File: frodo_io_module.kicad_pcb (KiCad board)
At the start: 4 copper layers, 60 x 60 mm, 174 parts, among them J1 Conn_02x04_Top_Bottom, J10 JST-GH 4Pin, J11 JST-GH 4Pin, J14 Conn_02x03_Odd_Even, J16 USB_C_Receptacle_USB2.0, J17 TC2050, J2 Conn_02x10_Odd_Even, J3 Conn_02x04_Top_Bottom, J4 Conn_02x03_Odd_Even, J5 Conn_02x04_Odd_Even, J6 JST-GH 4Pin, J7 JST-GH 4Pin, J8 JST-GH 4Pin, J9 JST-GH 4Pin, Q1 AOSP21321, Q2 AOSP21321, Q3 NMOS, Q4 NMOS, Q5 AOSP21321, Q6 AOSP21321, Q7 NMOS, Q8 NMOS, SW1 KMR721NGLFS, SW2 KMR721NGLFS, SW3 KMR721NGLFS, U1 L7805, U10 MCP2562-E-SN, U11 TPD4E1U06, U12 INA181A1, U2 L7805, U3 STM32F105RCTx, U4 AZ1117H-ADJ, U5 AZ1117H-ADJ, U6 W25Q128JVP, U7 MCP2562-E-SN, U8 TPD4E1U06, U9 INA181A1, Y1 8MHz 12pF

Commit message: rough placement of the components
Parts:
- C29, D10, D12, D13, D14, D16, D18, D19, D9, F2, F3, FB10, FB12, FB13, FB2, FB3, FB5, FB6, FB9, J17, Q1, Q2, Q3, Q4, Q5, Q6, Q7, Q8, R15, R17, R26, R30, R32, R33, R4, R41, R46, R47, R5, R52, R53, R54, R55, R56, R57, R58, R59, R60, R61, R62, R63, SW1, SW2, SW3, U11: moved to B.Cu
- moved D11 188.4 mm to (103.8, 137.7), turned to 90 degrees
- moved D7 186.7 mm to (103.8, 148.0), turned to 90 degrees
- moved U6 184.7 mm to (127.0, 141.4)
- moved D6 182.5 mm to (107.4, 140.5)
- moved D5 180.9 mm to (103.8, 127.8), turned to 90 degrees
- moved D9 168.1 mm to (114.1, 106.3), turned to 90 degrees
- moved D8 165.6 mm to (115.5, 134.1), turned to 90 degrees
- moved D14 164.2 mm to (141.0, 142.3), turned to -90 degrees
- moved D10 164.1 mm to (115.9, 106.4), turned to 90 degrees
- moved D13 163.6 mm to (141.7, 136.8)
- moved D3 161.3 mm to (103.7, 119.1), turned to 90 degrees
- moved D12 157.3 mm to (117.6, 106.4), turned to 90 degrees
- moved C1 154.2 mm to (124.0, 131.9), turned to 90 degrees
- moved D2 151.3 mm to (117.4, 115.7), turned to 90 degrees
- moved C22 150.7 mm to (128.7, 145.6)
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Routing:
- net Net-(D8-A): track 0.00 -> 21.1 mm
- net NRST: track 11.7 -> 0.00 mm
- net /VBUS: track 12.8 -> 6.15 mm
- net USB_D-: track 0.00 -> 5.91 mm
- net USB_D+: track 0.00 -> 5.91 mm
- net GND: track 10.2 -> 5.59 mm
- net Net-(U5-GND): track 0.00 -> 3.89 mm
- net unconnected-(J16-SBU2-PadB8): track 3.79 -> 0.00 mm
- net /D0+: track 3.83 -> 7.32 mm, vias 1 -> 2
- net +3.3V: track 16.8 -> 14.6 mm
- net Net-(J16-CC1): track 0.00 -> 1.92 mm, vias 0 -> 1
- net Net-(D11-A): track 0.00 -> 1.58 mm
- net Net-(J16-CC2): track 0.76 -> 2.22 mm
- net /D0-: track 8.54 -> 7.46 mm
- net (no net): track 0.99 -> 0.00 mm
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
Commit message: basic routing
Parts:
- C1, C10, C2, C20, C21, C22, C26, C3, C4, C5, C6, C7, C8, C9, D11, D3, D5, D7, FB1, FB11, FB4, FB7, FB8, R10, R11, R12, R13, R14, R18, R19, R20, R21, R22, R23, R25, R27, R31, R35, R36, R38, R39, R42, R48, R8, R9, U12, U3, U6, U8, U9, Y1: moved to B.Cu
- D13, D14, D16, D18, D19, F2, F3, J2, Q1, Q2, Q3, Q4, Q5, Q6, Q7, Q8, R15, R17, R4, R5, R52, R53, R55, R57, R58, R59, R60, R61, R62, R63: moved to F.Cu
- moved D7 42.9 mm to (119.0, 107.8), turned to -90 degrees
- moved C18 35.7 mm to (102.6, 148.0)
- moved D11 32.8 mm to (117.5, 107.8), turned to -90 degrees
- moved C22 32.2 mm to (127.0, 113.4), turned to 90 degrees
- moved R18 32.1 mm to (107.5, 128.1), turned to 90 degrees
- moved R19 31.7 mm to (107.4, 148.2), turned to 90 degrees
- moved R21 31.5 mm to (107.5, 122.0), turned to -90 degrees
- moved R13 29.9 mm to (107.5, 131.8), turned to -90 degrees
- moved C15 28.4 mm to (138.5, 105.1)
- moved C28 27.3 mm to (110.8, 111.8), turned to 0 degrees
- moved U6 26.3 mm to (123.4, 115.3), turned to 90 degrees
- moved R22 25.3 mm to (107.4, 141.9), turned to -90 degrees
- moved R31 24.7 mm to (119.1, 134.2), turned to 180 degrees
- moved C30 24.6 mm to (118.0, 136.2), turned to 180 degrees
- moved D5 23.4 mm to (116.0, 107.8), turned to -90 degrees
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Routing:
- net CAN_2_L: track 0.00 -> 110.1 mm, vias 0 -> 1
- net /Digital Output/OUT2: track 0.00 -> 107.2 mm, vias 0 -> 2
- net /Digital Output1/OUT1: track 0.00 -> 91.2 mm, vias 0 -> 2
- net CAN_2_H: track 0.00 -> 88.3 mm, vias 0 -> 3
- net /Digital Output1/OUT2: track 0.00 -> 88.0 mm, vias 0 -> 1
- net /Digital Output/OUT1: track 0.00 -> 84.0 mm, vias 0 -> 2
- net SWCLK: track 0.00 -> 73.3 mm, vias 0 -> 2
- net CAN_1_L: track 0.00 -> 64.2 mm, vias 0 -> 1
- net BOOT: track 0.00 -> 62.3 mm, vias 0 -> 3
- net CAN_1_H: track 0.00 -> 62.3 mm, vias 0 -> 1
- net NRST: track 0.00 -> 60.4 mm, vias 0 -> 5
- net COM4_1: track 0.00 -> 54.2 mm, vias 0 -> 2
- net Net-(D7-A): track 0.00 -> 53.6 mm, vias 0 -> 2
- net SWDIO: track 0.00 -> 48.9 mm
- net COM1_2: track 0.00 -> 48.7 mm, vias 0 -> 2
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
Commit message: more routing
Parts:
- moved R62 4.32 mm to (118.3, 124.5), turned to 180 degrees
- moved C25 2.86 mm to (123.3, 113.8)
- moved C11 2.40 mm to (112.5, 121.4)
- moved Q3 1.49 mm to (129.3, 123.4)
- moved J2 1.28 mm to (130.9, 115.9)
- moved D18 1.13 mm to (118.8, 143.2)
- moved D2 0.61 mm to (115.3, 119.0)
- moved R37 0.50 mm to (132.4, 104.1)
- moved D19 0.48 mm to (115.1, 157.0)
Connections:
- D13 pad 1: v_main_pre_sense -> main_voltage
- D14 pad 1: v_main_pre_sense -> main_voltage
- U3 pad 24: AIN2 -> AIN3
- U3 pad 25: AIN3 -> AIN2
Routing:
- net /Digital Output1/OUT1: track 91.2 -> 68.5 mm, vias 2 -> 3
- net CAN_2_L: track 110.1 -> 87.9 mm, vias 1 -> 3
- net CAN_2_H: track 88.3 -> 67.6 mm, vias 3 -> 0
- net NRST: track 60.4 -> 78.6 mm, vias 5 -> 10
- net COM2_1: track 31.6 -> 48.8 mm
- net COM4_2: track 48.1 -> 63.4 mm, vias 2 -> 0
- net SPI_CS_FLASH: track 0.00 -> 14.9 mm, vias 0 -> 2
- net STAT_LED0: track 48.4 -> 34.2 mm
- net /Digital Output1/OUT2: track 88.0 -> 101.4 mm, vias 1 -> 3
- net STAT_LED1: track 48.0 -> 35.8 mm
- net COM4_1: track 54.2 -> 64.9 mm, vias 2 -> 0
- net AIN1: track 11.6 -> 20.8 mm
- net SWO: track 41.2 -> 46.7 mm
- net CAN_1_L: track 64.2 -> 68.7 mm, vias 1 -> 2
- net COM2_2: track 30.0 -> 25.9 mm
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
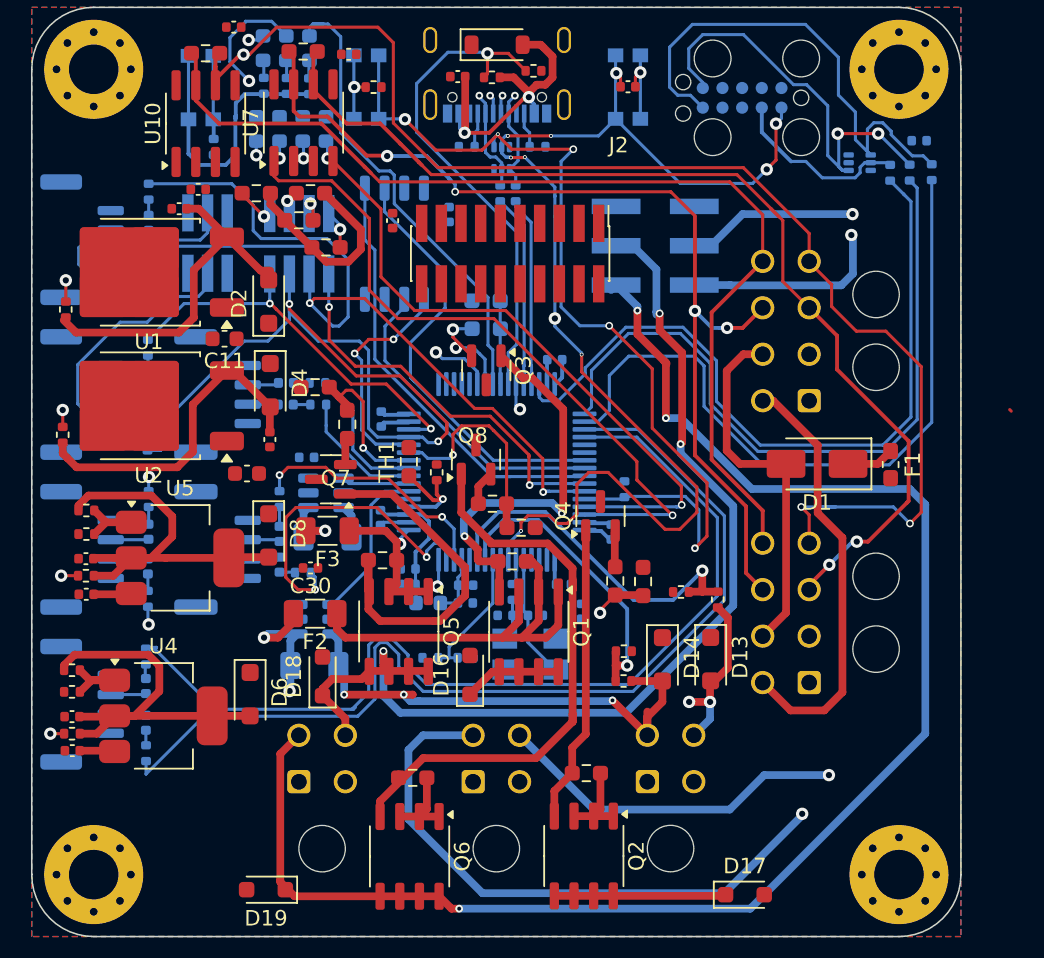
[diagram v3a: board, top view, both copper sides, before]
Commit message: remove second 3.3V reg and i2c pull up jumpers
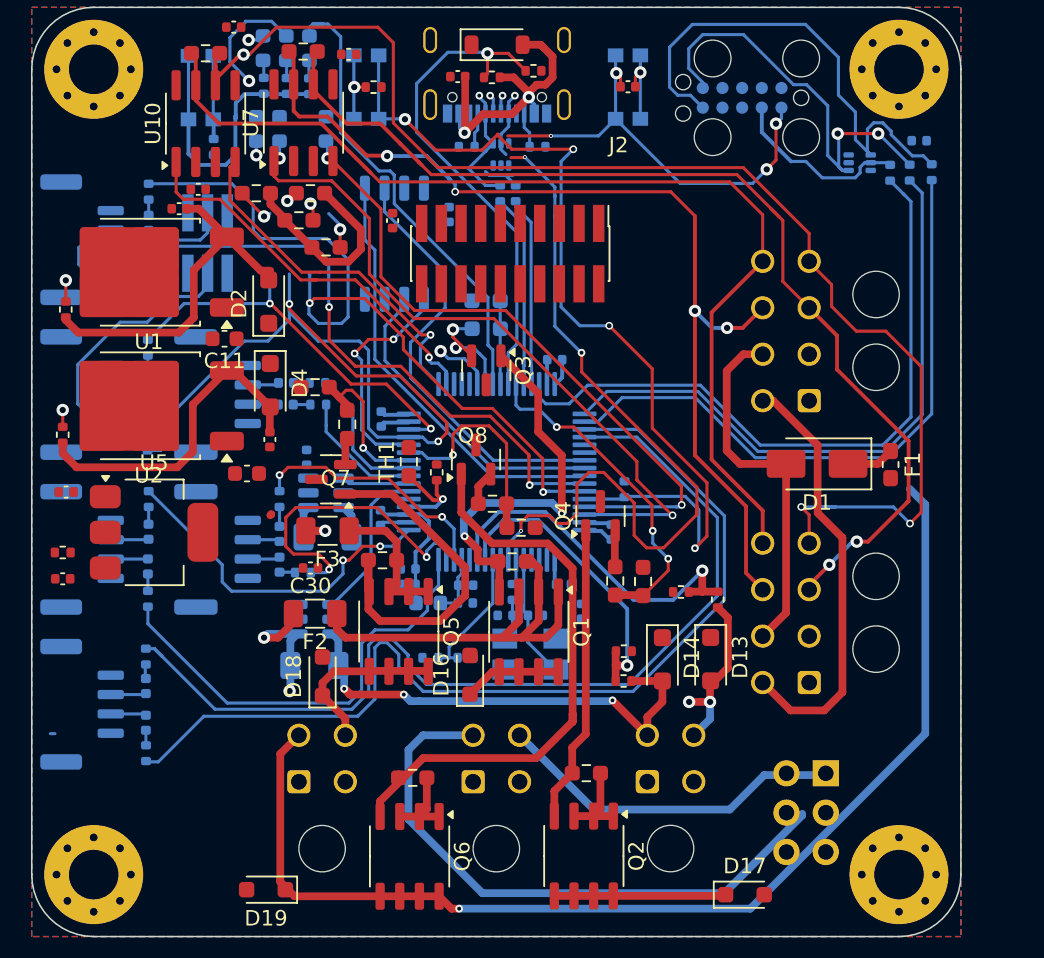
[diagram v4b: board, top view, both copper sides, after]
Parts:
- removed C18: 10u, Capacitor_SMD:C_0402_1005Metric
- removed C19: 22u, Capacitor_SMD:C_0402_1005Metric
- removed D11: red, LED_SMD:LED_0603_1608Metric
- removed D6, D8: RB070MM-30TR, Diode_SMD:D_SOD-123F
- removed J5: Conn_02x04_Odd_Even, Connector_PinHeader_1.27mm:PinHeader_2x04_P1.27mm_Vertical_SMD
- removed R15, R24: 150R, Resistor_SMD:R_0402_1005Metric
- removed R17, R29: 300, Resistor_SMD:R_0402_1005Metric
- removed R28: 220, Resistor_SMD:R_0402_1005Metric
- removed U4: AZ1117H-ADJ, Package_TO_SOT_SMD:SOT-223-3_TabPin2
- J14: footprint Connector_PinHeader_2.54mm:PinHeader_2x03_P2.54mm_Vertical_SMD -> Connector_PinHeader_2.54mm:PinHeader_2x03_P2.54mm_Vertical
- U5: value AZ1117H-ADJ -> AZ1117-3.3
- moved J14 35.8 mm to (151.3, 149.5)
- moved C17 14.5 mm to (102.2, 131.3)
- moved R16 11.7 mm to (102.0, 135.2)
- moved U5 2.35 mm to (107.9, 133.9)
- moved C16 1.82 mm to (102.0, 136.9)
- moved U8 0.24 mm to (130.3, 109.5), turned to 90 degrees
- turned C26 to 90 degrees
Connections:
- C17 pad 2: Net-(D6-A) -> +3.3V
- R16 pad 1: Net-(D6-A) -> +3.3V
- R4 pad 2: Net-(J5-Pin_2) -> Net-(FB2-Pad1)
- R5 pad 1: +3.3V -> Net-(FB5-Pad1)
- R5 pad 2: Net-(J5-Pin_4) -> +3.3V
- R6 pad 2: Net-(J5-Pin_6) -> Net-(FB8-Pad1)
- R7 pad 1: +3.3V -> Net-(FB11-Pad1)
- R7 pad 2: Net-(J5-Pin_8) -> +3.3V
- U5 pad 1: Net-(U5-GND) -> GND
- U5 pad 2: Net-(D8-A) -> +3.3V
- U8 pad 4: /D0+ -> /D0-
- U8 pad 5: /D0- -> /D0+
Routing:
- net /Digital Output/OUT2: track 107.2 -> 49.7 mm, vias 2 -> 0
- net /Digital Output1/OUT1: track 68.5 -> 11.1 mm, vias 3 -> 0
- net /Digital Output/OUT1: track 84.0 -> 29.2 mm, vias 2 -> 0
- net Net-(D11-A): track 41.2 -> 0.00 mm, vias 2 -> 0
- net /Digital Output1/OUT2: track 101.4 -> 73.2 mm, vias 3 -> 1
- net Net-(D8-A): track 28.2 -> 0.00 mm
- net Net-(D6-A): track 26.7 -> 0.00 mm
- net CAN2_TX: track 0.00 -> 25.6 mm, vias 0 -> 1
- net CAN2_RX: track 0.00 -> 23.1 mm, vias 0 -> 1
- net COM3_1: track 22.8 -> 29.1 mm, vias 2 -> 0
- net SWO: track 46.7 -> 40.9 mm
- net SWCLK: track 73.3 -> 67.6 mm
- net Net-(U4-GND): track 5.06 -> 0.00 mm
- net +5V: track 4.72 -> 0.00 mm
- net SWDIO: track 48.9 -> 44.2 mm
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
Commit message: more routing
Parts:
- C30: moved to B.Cu
- R27, R31, R54, R56: moved to F.Cu
- moved Q8 23.4 mm to (107.6, 139.4), turned to 180 degrees
- moved U12 22.3 mm to (140.4, 137.5)
- moved Q4 22.1 mm to (145.2, 153.2), turned to 0 degrees
- moved R31 21.8 mm to (140.6, 137.7)
- moved C26 21.0 mm to (135.5, 140.4), turned to -90 degrees
- moved R55 20.7 mm to (144.4, 156.7)
- moved R57 20.7 mm to (146.2, 156.7)
- moved R27 19.9 mm to (138.2, 142.3)
- moved U9 19.9 mm to (138.1, 141.5)
- moved C30 19.8 mm to (137.8, 137.1), turned to -90 degrees
- moved F3 17.2 mm to (135.9, 137.6), turned to 0 degrees
- moved R61 16.8 mm to (113.3, 135.7), turned to -90 degrees
- moved R59 16.7 mm to (111.2, 139.8)
- moved Q6 16.0 mm to (112.3, 144.4)
- moved R63 15.9 mm to (115.8, 132.9)
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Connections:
- U3 pad 14: AIN0 -> I_sense_1
- U3 pad 15: AIN1 -> I_sense_2
- U3 pad 22: I_sense_1 -> AIN1
- U3 pad 23: I_sense_2 -> AIN0
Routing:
- net /Digital Output1/OUT1: track 11.1 -> 46.4 mm
- net Net-(Q6-G): track 38.0 -> 3.95 mm
- net /Digital Output/VD: track 31.3 -> 2.70 mm
- net /Digital Output1/VD: track 14.6 -> 42.8 mm
- net SH11: track 32.1 -> 5.43 mm, vias 3 -> 4
- net Net-(Q1-G): track 25.2 -> 2.25 mm, vias 2 -> 0
- net HC_OUT_2: track 21.6 -> 44.4 mm, vias 3 -> 1
- net COM2_1: track 48.8 -> 26.0 mm, vias 2 -> 0
- net I_sense_2: track 4.35 -> 26.7 mm, vias 0 -> 2
- net Net-(Q5-G): track 24.0 -> 2.19 mm
- net /Digital Output1/OUT2: track 73.2 -> 52.1 mm, vias 1 -> 0
- net Net-(Q2-G): track 19.3 -> 2.24 mm
- net /Digital Output/OUT1: track 29.2 -> 45.3 mm
- net Net-(Q7-G): track 1.74 -> 17.6 mm, vias 0 -> 2
- net Net-(Q3-G): track 3.46 -> 18.9 mm, vias 1 -> 2
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- added copper zone on F.Cu, net (none)
- added copper zone on F.Cu, net /Digital Output/VD
- added copper zone on B.Cu, net SH11
- added copper zone on B.Cu, net SH12
- added copper zone on B.Cu, net SH21
- added copper zone on B.Cu, net SH22

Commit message: more routing
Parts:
- R5: moved to B.Cu
- moved R57 28.2 mm to (129.5, 134.0), turned to -90 degrees
- moved R55 28.0 mm to (128.0, 134.0), turned to -90 degrees
- moved Q4 27.4 mm to (125.5, 134.3), turned to 90 degrees
- moved R6 22.6 mm to (106.2, 131.3), turned to 0 degrees
- moved D17 19.9 mm to (123.2, 148.8), turned to -90 degrees
- moved R1 15.3 mm to (116.5, 114.0), turned to -90 degrees
- moved Q2 14.9 mm to (126.3, 141.6)
- moved R53 14.6 mm to (125.5, 137.1)
- moved R50 14.4 mm to (145.2, 150.2), turned to -90 degrees
- moved R7 13.7 mm to (104.1, 121.0)
- moved R44 11.6 mm to (145.1, 148.1), turned to -90 degrees
- moved R4 11.4 mm to (109.0, 121.0), turned to 180 degrees
- moved R54 11.3 mm to (136.1, 132.3)
- moved R5 11.2 mm to (107.1, 108.9)
- moved R56 11.0 mm to (132.7, 132.3), turned to 180 degrees
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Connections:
- J2 pad 11: IO-3 (ADC) -> SPI1_SCK
- J2 pad 12: IO-6 -> IO-8
- J2 pad 14: IO-7 -> IO-3 (ADC)
- J2 pad 15: IO-4 -> SPI1_MISO
- J2 pad 16: IO-8 -> IO-5
- J2 pad 17: IO-5 -> GND
- J2 pad 18: GND -> IO-4
- J2 pad 4: SPI1_SCK -> IO-1 (UART5 RX)
- J2 pad 5: IO-0 (UART5 TX) -> IO-6
- J2 pad 6: SPI1_MISO -> IO-0 (UART5 TX)
- J2 pad 7: IO-1 (UART5 RX) -> IO-7
- J2 pad 8: SPI1_MOSI -> IO-2 (ADC/DAC)
- J2 pad 9: IO-2 (ADC/DAC) -> SPI1_MOSI
- U3 pad 10: hc_sense -> hc2_sense
- U3 pad 11: hc2_sense -> hc_sense
- U3 pad 4: IO-8 -> HC_OUT_2
- U3 pad 41: HC_OUT_1 -> IO-3 (ADC)
- U3 pad 43: HC_OUT_2 -> IO-8
- U3 pad 51: COM4_1 -> IO-0 (UART5 TX)
- U3 pad 52: COM4_2 -> IO-1 (UART5 RX)
- U3 pad 53: IO-0 (UART5 TX) -> COM4_1
- U3 pad 54: IO-1 (UART5 RX) -> COM4_2
- U3 pad 8: IO-3 (ADC) -> HC_OUT_1
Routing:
- net hc_sense: track 17.7 -> 60.4 mm
- net IO-2 (ADC/DAC): track 0.00 -> 42.2 mm, vias 0 -> 5
- net IO-6: track 0.00 -> 40.3 mm, vias 0 -> 2
- net IO-7: track 0.00 -> 39.4 mm, vias 0 -> 2
- net HC_OUT_2: track 44.4 -> 6.53 mm
- net +5V: track 0.00 -> 33.9 mm
- net SWITCH: track 5.38 -> 34.7 mm
- net I_sense_1: track 24.1 -> 52.1 mm, vias 2 -> 4
- net /Digital Output/VD: track 2.70 -> 22.2 mm
- net hc2_sense: track 19.1 -> 37.2 mm
- net I_sense_2: track 26.7 -> 44.8 mm, vias 2 -> 4
- net Net-(D2-A): track 22.3 -> 5.69 mm
- net Net-(Q3-G): track 18.9 -> 2.28 mm, vias 2 -> 0
- net Net-(Q7-G): track 17.6 -> 1.81 mm, vias 2 -> 0
- net IO-1 (UART5 RX): track 0.00 -> 15.5 mm, vias 0 -> 1
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- removed copper zone on F.Cu, net (none)
- removed copper zone on F.Cu, net /Digital Output/VD
- removed copper zone on B.Cu, net SH11
- removed copper zone on B.Cu, net SH12
- removed copper zone on B.Cu, net SH21
- removed copper zone on B.Cu, net SH22

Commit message: power routing
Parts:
- C29: moved to F.Cu
- moved C22 6.57 mm to (121.6, 109.6), turned to 0 degrees
- moved C29 4.79 mm to (152.9, 109.4)
- moved R52 1.30 mm to (136.5, 138.8)
- moved J14 0.94 mm to (151.1, 150.4)
- moved R46 0.63 mm to (157.5, 110.7)
- moved R3 0.36 mm to (102.4, 127.6)
- moved C27 0.25 mm to (114.0, 103.3)
- moved R47 0.22 mm to (156.5, 110.7)
- moved D4 0.15 mm to (115.2, 124.4)
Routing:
- net +3.3V: track 51.4 -> 378.4 mm, vias 0 -> 23
- net main_voltage: track 4.38 -> 185.0 mm, vias 0 -> 3
- net +5V: track 33.9 -> 163.6 mm, vias 0 -> 6
- net /VBUS: track 21.4 -> 30.4 mm, vias 2 -> 3
- net IO-7: track 39.4 -> 45.8 mm
- net /Digital Output/VD: track 22.2 -> 27.7 mm
- net IO-6: track 40.3 -> 45.7 mm
- net /Digital Output1/OUT1: track 43.7 -> 47.5 mm
- net /Digital Output1/VD: track 48.4 -> 51.1 mm
- net CAN_2_L: track 88.2 -> 85.6 mm
- net I_sense_2: track 44.8 -> 46.9 mm
- net Net-(Q1-G): track 2.85 -> 4.98 mm
- net /Digital Output1/OUT2: track 54.1 -> 52.3 mm
- net I_sense_1: track 52.1 -> 53.8 mm
- net hc2_sense: track 37.2 -> 38.8 mm
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
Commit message: finish routing
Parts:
- moved J2 2.59 mm to (129.7, 116.3)
- moved R14 2.22 mm to (116.0, 137.9), turned to 90 degrees
- moved R56 0.81 mm to (131.9, 132.3)
- moved R54 0.81 mm to (135.3, 132.3)
- moved C6 0.70 mm to (138.1, 133.9)
- moved R2 0.63 mm to (121.5, 105.4)
- moved R27 0.47 mm to (139.7, 140.7)
- moved R38 0.44 mm to (129.1, 112.5)
- moved R39 0.44 mm to (130.1, 112.5)
- moved Y1 0.40 mm to (131.8, 141.8)
- moved C25 0.38 mm to (114.4, 108.1)
- moved F2 0.36 mm to (139.8, 135.9)
- moved R11 0.26 mm to (116.0, 132.0)
- moved R31 0.23 mm to (143.4, 140.7)
- moved F3 0.23 mm to (143.4, 135.8)
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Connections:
- J17 pad 6: SWCLK -> /J1-SWCLK
- J2 pad 13: GND -> SPI1_MISO
- J2 pad 15: SPI1_MISO -> GND
- J2 pad 16: IO-5 -> IO-4
- J2 pad 18: IO-4 -> IO-5
- J2 pad 5: IO-6 -> IO-7
- J2 pad 7: IO-7 -> IO-6
- R47 pad 1: SWCLK -> /J1-SWCLK
- U11 pad 4: SWCLK -> /J1-SWCLK
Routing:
- net GND: track 17.1 -> 168.5 mm, vias 1 -> 69
- net SWCLK: track 56.1 -> 28.4 mm, vias 2 -> 0
- net /J1-SWCLK: track 0.00 -> 26.3 mm, vias 0 -> 2
- net /Digital Output1/VD: track 51.1 -> 33.0 mm
- net /Digital Output/VD: track 27.7 -> 10.9 mm
- net /Digital Output1/OUT1: track 47.5 -> 34.0 mm
- net IO-6: track 45.7 -> 57.4 mm, vias 2 -> 1
- net /Digital Output/OUT2: track 51.4 -> 41.1 mm
- net /Digital Output/OUT1: track 44.0 -> 33.8 mm
- net +3.3V: track 378.4 -> 368.6 mm, vias 23 -> 24
- net IO-7: track 45.8 -> 55.1 mm, vias 2 -> 1
- net /Digital Output1/OUT2: track 52.3 -> 48.1 mm
- net +5V: track 163.6 -> 167.6 mm
- net hc_sense: track 59.3 -> 63.2 mm
- net CAN_2_L: track 85.6 -> 82.8 mm
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- added copper zone on F.Cu, net +3.3V
- added copper zone on F.Cu, net /Digital Output/OUT1
- added copper zone on F.Cu, net /Digital Output/OUT2
- added copper zone on F.Cu, net /Digital Output/VD
- added copper zone on F.Cu, net /Digital Output1/OUT1
- added copper zone on F.Cu, net /Digital Output1/OUT2
- added copper zone on F.Cu, net /Digital Output1/VD
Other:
- board text added: "4"
- board text added: "4 COM1 5 COM2 6 COM3 7 COM4 8 COM5 9 COM6"
- board text added: "5"
- board text added: "6"
- board text added: "7"
- board text added: "8"
- board text added: "9"
- board text removed: "COM1"
- board text removed: "COM2"
- board text removed: "COM3"
- board text removed: "COM4"
